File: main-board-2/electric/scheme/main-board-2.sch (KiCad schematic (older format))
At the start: 125 parts, among them K1 power-switch, K2 usb-power-switch, P1 batt, P10 rst, P11 screw-1, P13 screw-2, P14 gpio-big, P15 gpio-small, P16 moto-1, P17 moto-2, P2 CONN_4, P3 trigger-btn, P4 CONN_3X2, P5 reg-short-to-gnd-1, P6 reg-short-to-gnd-2, P7 bootloader, P8 cross board conn, P9 rst, Q1 IRLML2244, Q10 IRLML2244, Q11 sot223, Q12 bc857, Q13 irlml2244, Q2 BC847, Q3 IRLML2244, Q4 IRLML2244, Q5 BC847, Q6 BC847, Q7 BC847, Q8 BC847, Q9 IRLML2244, U1 LM317AEMP, U2 LM317AT, U3 LM317AEMP, U4 LM317AT, U5 LM293, U6 L298, U7 MINI-USB-B, X1 8MHz

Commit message: Routing...
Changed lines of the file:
@@
 Sheet 1 1
 Title "Main board 2"
-Date "9 dec 2013"
+Date "10 dec 2013"
 Rev ""
 Comp ""
@@
 Text Label 17650 4000 0    60   ~ 0
 gnd
-Text Label 14400 7700 0    60   ~ 0
+Text Label 14400 9650 0    60   ~ 0
 gpio-1
-Text Label 14600 4750 0    60   ~ 0
+Text Label 14400 7700 0    60   ~ 0
 gpio-2
-Text Label 14600 4150 0    60   ~ 0
+Text Label 14600 4350 0    60   ~ 0
 gpio-3
-Text Label 14600 3750 0    60   ~ 0
+Text Label 14600 3950 0    60   ~ 0
 gpio-4
 Text Label 14400 10050 0    60   ~ 0
 gpio-5
-Text Label 14600 4550 0    60   ~ 0
+Text Label 14600 4750 0    60   ~ 0
 gpio-6
-Text Label 14600 4350 0    60   ~ 0
+Text Label 14600 4550 0    60   ~ 0
 gpio-7
-Text Label 14600 3950 0    60   ~ 0
+Text Label 14600 4150 0    60   ~ 0
 gpio-8
 Text Label 16150 3300 0    60   ~ 0
@@
 Text Label 17900 4500 0    60   ~ 0
 swd-io
-Text Label 14400 9650 0    60   ~ 0
+Text Label 14600 3750 0    60   ~ 0
 gpio-9
 Text Label 16150 4300 0    60   ~ 0

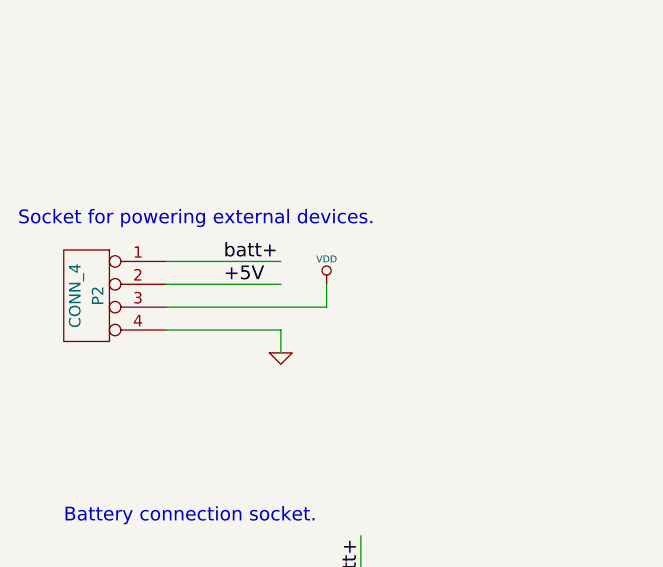
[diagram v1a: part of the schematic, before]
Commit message: Routing. It turnes out it is very nontrivial to route with horizontal TO-220. I'm going to change to vertical TO-220.
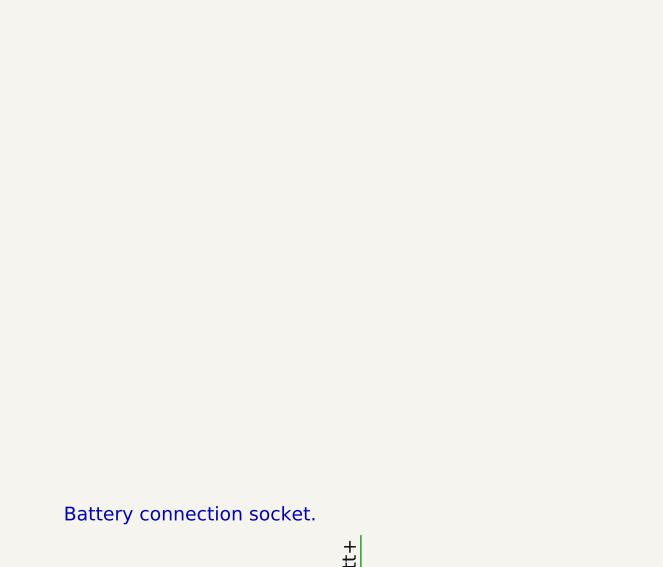
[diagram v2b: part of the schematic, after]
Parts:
- removed P2: CONN_4, symbol CONN_4
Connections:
- wire segments 423 -> 417
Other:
- note removed: "Socket for powering external devices."
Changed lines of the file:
@@
 Text Notes 11300 12800 0    60   ~ 0
 Two unconnected pins for screws.\nThe newest Raspberry Pi contains \nholes for M2.5 screws.
-$Comp
-L CONN_4 P2
-U 1 1 52A0D56C
-P 1350 19950
-F 0 "P2" V 1300 19950 50  0000 C CNN
-F 1 "CONN_4" V 1400 19950 50  0000 C CNN
-F 2 "" H 1350 19950 60  0001 C CNN
-F 3 "" H 1350 19950 60  0001 C CNN
-	1    1350 19950
-	-1   0    0    -1
-$EndComp
-Wire Wire Line
-	1700 19800 2200 19800
-Wire Wire Line
-	1700 19900 2200 19900
-Wire Wire Line
-	1700 20000 2400 20000
-Wire Wire Line
-	1700 20100 2200 20100
-Wire Wire Line
-	2200 20100 2200 20200
-$Comp
-L GND #PWR032
-U 1 1 52A0D577
-P 2200 20200
-F 0 "#PWR032" H 2200 20200 30  0001 C CNN
-F 1 "GND" H 2200 20130 30  0001 C CNN
-F 2 "" H 2200 20200 60  0001 C CNN
-F 3 "" H 2200 20200 60  0001 C CNN
-	1    2200 20200
-	1    0    0    -1
-$EndComp
-Wire Wire Line
-	2400 20000 2400 19900
-$Comp
-L VDD #PWR033
-U 1 1 52A0D57E
-P 2400 19900
-F 0 "#PWR033" H 2400 20000 30  0001 C CNN
-F 1 "VDD" H 2400 20010 30  0000 C CNN
-F 2 "" H 2400 19900 60  0001 C CNN
-F 3 "" H 2400 19900 60  0001 C CNN
-	1    2400 19900
-	1    0    0    -1
-$EndComp
-Text Label 1950 19800 0    60   ~ 0
-batt+
-Text Label 1950 19900 0    60   ~ 0
-+5V
-Text Notes 1050 19650 0    60   ~ 0
-Socket for powering external devices.
 Wire Wire Line
 	14100 7700 15100 7700

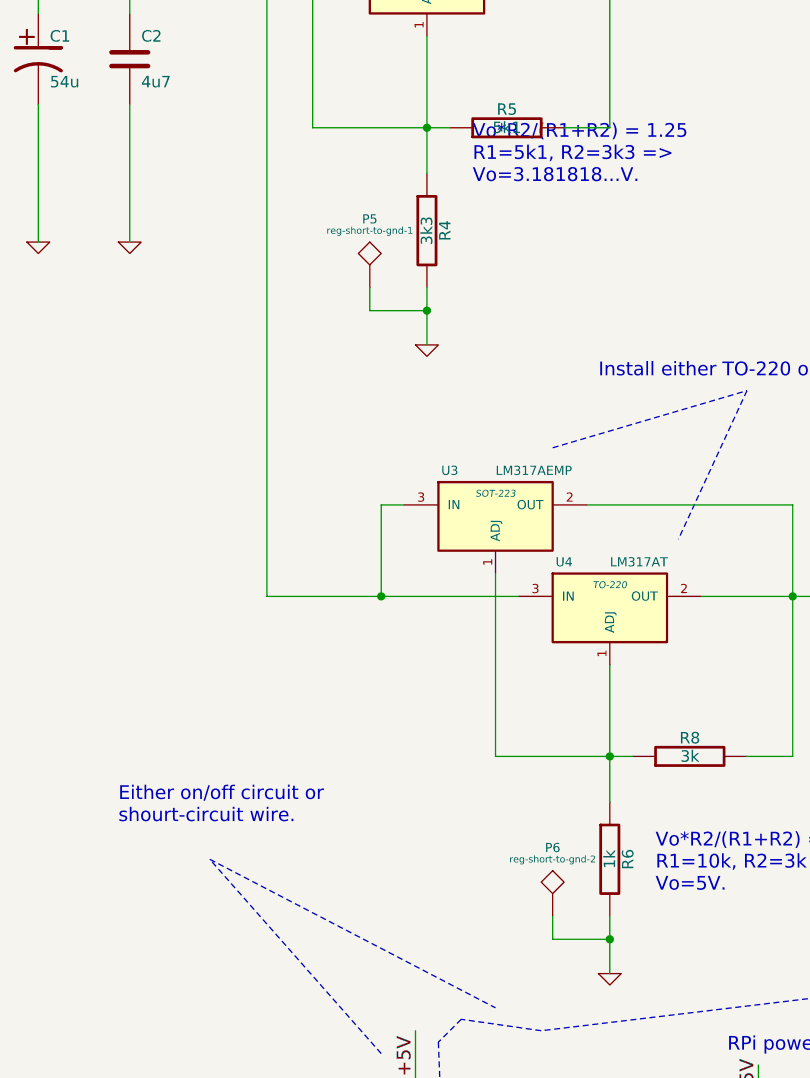
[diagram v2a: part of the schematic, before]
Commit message: Just one more circuit Vdd to addon socket last.
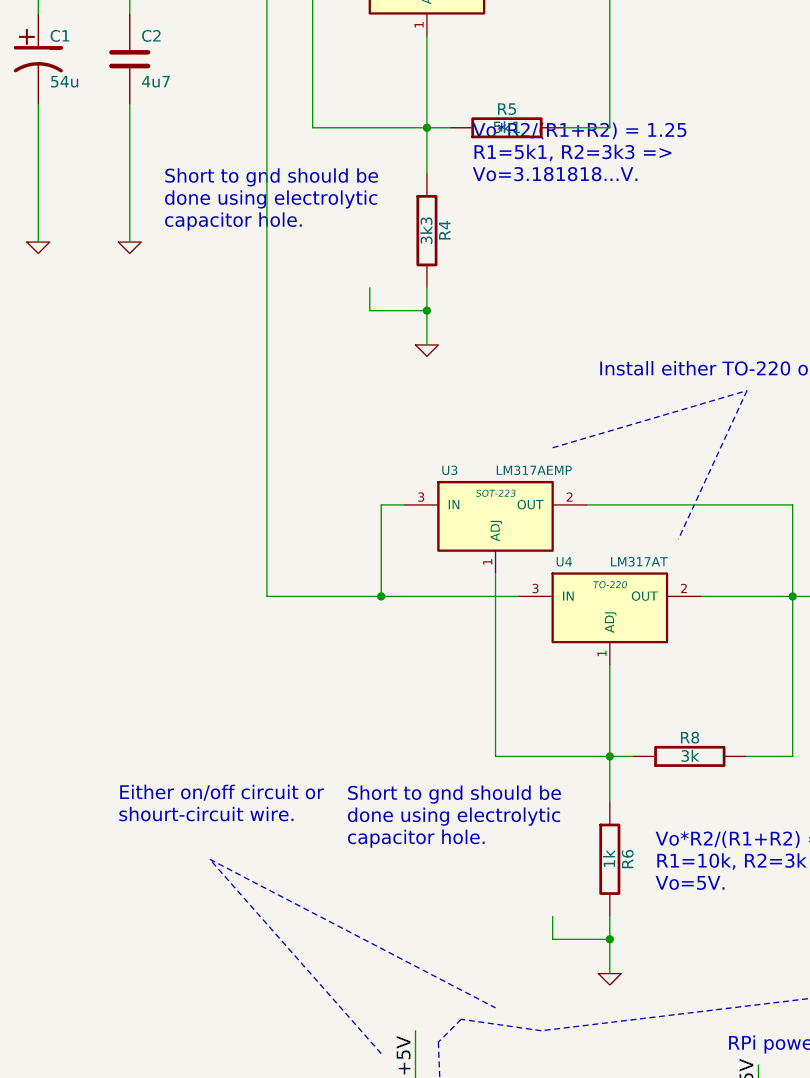
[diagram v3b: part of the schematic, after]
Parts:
- removed P5: reg-short-to-gnd-1, ~, symbol TST
- removed P6: reg-short-to-gnd-2, ~, symbol TST
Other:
- note added: "Short to gnd should be \ndone using electrolytic \ncapacitor hole."
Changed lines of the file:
@@
 Sheet 1 1
 Title "Main board 2"
-Date "10 dec 2013"
+Date "11 dec 2013"
 Rev ""
 Comp ""
@@
 	9450 2500 9450 2600
 $Comp
-L GND #PWR034
+L GND #PWR032
 U 1 1 52A0D5D0
 P 9450 2600
-F 0 "#PWR034" H 9450 2600 30  0001 C CNN
+F 0 "#PWR032" H 9450 2600 30  0001 C CNN
 F 1 "GND" H 9450 2530 30  0001 C CNN
 F 2 "" H 9450 2600 60  0001 C CNN
@@
 	8200 7750 8200 7600
 $Comp
-L VDD #PWR035
+L VDD #PWR033
 U 1 1 52A0E8C5
 P 8200 7600
-F 0 "#PWR035" H 8200 7700 30  0001 C CNN
+F 0 "#PWR033" H 8200 7700 30  0001 C CNN
 F 1 "VDD" H 8200 7710 30  0000 C CNN
 F 2 "" H 8200 7600 60  0001 C CNN
@@
 +5V
 $Comp
-L GND #PWR036
+L GND #PWR034
 U 1 1 52A0FADE
 P 13250 20350
-F 0 "#PWR036" H 13250 20350 30  0001 C CNN
+F 0 "#PWR034" H 13250 20350 30  0001 C CNN
 F 1 "GND" H 13250 20280 30  0001 C CNN
 F 2 "" H 13250 20350 60  0001 C CNN
@@
 addon-vdd
 $Comp
-L VDD #PWR037
+L VDD #PWR035
 U 1 1 52A0FB08
 P 13250 18850
-F 0 "#PWR037" H 13250 18950 30  0001 C CNN
+F 0 "#PWR035" H 13250 18950 30  0001 C CNN
 F 1 "VDD" H 13250 18960 30  0000 C CNN
 F 2 "" H 13250 18850 60  0001 C CNN
@@
 Connection ~ 14300 19000
 $Comp
-L VDD #PWR038
+L VDD #PWR036
 U 1 1 52A105F2
 P 11950 19150
-F 0 "#PWR038" H 11950 19250 30  0001 C CNN
+F 0 "#PWR036" H 11950 19250 30  0001 C CNN
 F 1 "VDD" H 11950 19260 30  0000 C CNN
 F 2 "" H 11950 19150 60  0001 C CNN
@@
 $EndComp
 $Comp
-L GND #PWR039
+L GND #PWR037
 U 1 1 52A1147D
 P 1300 2800
-F 0 "#PWR039" H 1300 2800 30  0001 C CNN
+F 0 "#PWR037" H 1300 2800 30  0001 C CNN
 F 1 "GND" H 1300 2730 30  0001 C CNN
 F 2 "" H 1300 2800 60  0001 C CNN
@@
 $EndComp
 $Comp
-L GND #PWR040
+L GND #PWR038
 U 1 1 52A12B15
 P 5300 5200
-F 0 "#PWR040" H 5300 5200 30  0001 C CNN
+F 0 "#PWR038" H 5300 5200 30  0001 C CNN
 F 1 "GND" H 5300 5130 30  0001 C CNN
 F 2 "" H 5300 5200 60  0001 C CNN
@@
 $EndComp
 $Comp
-L GND #PWR041
+L GND #PWR039
 U 1 1 52A12B21
 P 4950 5200
-F 0 "#PWR041" H 4950 5200 30  0001 C CNN
+F 0 "#PWR039" H 4950 5200 30  0001 C CNN
 F 1 "GND" H 4950 5130 30  0001 C CNN
 F 2 "" H 4950 5200 60  0001 C CNN
@@
 $EndComp
 $Comp
-L GND #PWR042
+L GND #PWR040
 U 1 1 52A12B2D
 P 3800 6000
-F 0 "#PWR042" H 3800 6000 30  0001 C CNN
+F 0 "#PWR040" H 3800 6000 30  0001 C CNN
 F 1 "GND" H 3800 5930 30  0001 C CNN
 F 2 "" H 3800 6000 60  0001 C CNN
@@
 	24000 5050 24000 5100
 $Comp
-L GND #PWR043
+L GND #PWR041
 U 1 1 52A1B75F
 P 24000 5100
-F 0 "#PWR043" H 24000 5100 30  0001 C CNN
+F 0 "#PWR041" H 24000 5100 30  0001 C CNN
 F 1 "GND" H 24000 5030 30  0001 C CNN
 F 2 "" H 24000 5100 60  0001 C CNN
@@
 Connection ~ 30050 5800
 $Comp
-L GND #PWR044
+L GND #PWR042
 U 1 1 52A1DEAF
 P 30050 6000
-F 0 "#PWR044" H 30050 6000 30  0001 C CNN
+F 0 "#PWR042" H 30050 6000 30  0001 C CNN
 F 1 "GND" H 30050 5930 30  0001 C CNN
 F 2 "" H 30050 6000 60  0001 C CNN
@@
 	23350 5850 23350 6000
 $Comp
-L GND #PWR045
+L GND #PWR043
 U 1 1 52A1EAE1
 P 23350 6000
-F 0 "#PWR045" H 23350 6000 30  0001 C CNN
+F 0 "#PWR043" H 23350 6000 30  0001 C CNN
 F 1 "GND" H 23350 5930 30  0001 C CNN
 F 2 "" H 23350 6000 60  0001 C CNN
@@
 $EndComp
 $Comp
-L GND #PWR046
+L GND #PWR044
 U 1 1 52A1A7C0
 P 20700 3450
-F 0 "#PWR046" H 20700 3450 30  0001 C CNN
+F 0 "#PWR044" H 20700 3450 30  0001 C CNN
 F 1 "GND" H 20700 3380 30  0001 C CNN
 F 2 "" H 20700 3450 60  0001 C CNN
@@
 	23350 4750 23350 4900
 $Comp
-L GND #PWR047
+L GND #PWR045
 U 1 1 52A1A7F0
 P 23350 4900
-F 0 "#PWR047" H 23350 4900 30  0001 C CNN
+F 0 "#PWR045" H 23350 4900 30  0001 C CNN
 F 1 "GND" H 23350 4830 30  0001 C CNN
 F 2 "" H 23350 4900 60  0001 C CNN
@@
 addon-pwr-en
 $Comp
-L PWR_FLAG #FLG048
+L PWR_FLAG #FLG046
 U 1 1 52A1DA8C
 P 23350 1800
-F 0 "#FLG048" H 23350 1895 30  0001 C CNN
+F 0 "#FLG046" H 23350 1895 30  0001 C CNN
 F 1 "PWR_FLAG" H 23350 1980 30  0000 C CNN
 F 2 "" H 23350 1800 60  0001 C CNN
@@
 Connection ~ 23050 5250
 $Comp
-L PWR_FLAG #FLG049
+L PWR_FLAG #FLG047
 U 1 1 52A1DD5E
 P 23050 5100
-F 0 "#FLG049" H 23050 5195 30  0001 C CNN
+F 0 "#FLG047" H 23050 5195 30  0001 C CNN
 F 1 "PWR_FLAG" H 23050 5280 30  0000 C CNN
 F 2 "" H 23050 5100 60  0001 C CNN
@@
 	28300 5050 28300 5150
 $Comp
-L GND #PWR050
+L GND #PWR048
 U 1 1 52A1EACD
 P 28300 5150
-F 0 "#PWR050" H 28300 5150 30  0001 C CNN
+F 0 "#PWR048" H 28300 5150 30  0001 C CNN
 F 1 "GND" H 28300 5080 30  0001 C CNN
 F 2 "" H 28300 5150 60  0001 C CNN
@@
 $EndComp
 $Comp
-L PWR_FLAG #FLG051
+L PWR_FLAG #FLG049
 U 1 1 52A1EEED
 P 24800 19400
-F 0 "#FLG051" H 24800 19495 30  0001 C CNN
+F 0 "#FLG049" H 24800 19495 30  0001 C CNN
 F 1 "PWR_FLAG" H 24800 19580 30  0000 C CNN
 F 2 "" H 24800 19400 60  0001 C CNN
@@
 $EndComp
 $Comp
-L GND #PWR052
+L GND #PWR050
 U 1 1 52A1ABD9
 P 4450 7900
-F 0 "#PWR052" H 4450 7900 30  0001 C CNN
+F 0 "#PWR050" H 4450 7900 30  0001 C CNN
 F 1 "GND" H 4450 7830 30  0001 C CNN
 F 2 "" H 4450 7900 60  0001 C CNN
@@
 $EndComp
 $Comp
-L GND #PWR053
+L GND #PWR051
 U 1 1 52A1AC0E
 P 5500 8200
-F 0 "#PWR053" H 5500 8200 30  0001 C CNN
+F 0 "#PWR051" H 5500 8200 30  0001 C CNN
 F 1 "GND" H 5500 8130 30  0001 C CNN
 F 2 "" H 5500 8200 60  0001 C CNN
@@
 Wire Wire Line
 	3300 4250 3300 5050
-$Comp
-L TST P5
-U 1 1 52A32BAB
-P 2750 3000
-F 0 "P5" H 2750 3300 40  0000 C CNN
-F 1 "reg-short-to-gnd-1" H 2750 3250 30  0000 C CNN
-F 2 "~" H 2750 3000 60  0000 C CNN
-F 3 "~" H 2750 3000 60  0000 C CNN
-	1    2750 3000
-	1    0    0    -1
-$EndComp
 Wire Wire Line
 	2750 3000 2750 3100
@@
 	2750 3100 3000 3100
 Connection ~ 3000 3100
-$Comp
-L TST P6
-U 1 1 52A32D31
-P 3550 5750
-F 0 "P6" H 3550 6050 40  0000 C CNN
-F 1 "reg-short-to-gnd-2" H 3550 6000 30  0000 C CNN
-F 2 "~" H 3550 5750 60  0000 C CNN
-F 3 "~" H 3550 5750 60  0000 C CNN
-	1    3550 5750
-	1    0    0    -1
-$EndComp
 Wire Wire Line
 	3550 5750 3550 5850
@@
 +5V
 $Comp
-L VDD #PWR054
+L VDD #PWR052
 U 1 1 52A348A1
 P 11700 18600
-F 0 "#PWR054" H 11700 18700 30  0001 C CNN
+F 0 "#PWR052" H 11700 18700 30  0001 C CNN
 F 1 "VDD" H 11700 18710 30  0000 C CNN
 F 2 "" H 11700 18600 60  0001 C CNN
@@
 Connection ~ 29850 19250
 $Comp
-L GND #PWR055
+L GND #PWR053
 U 1 1 52A36BFA
 P 29850 20300
-F 0 "#PWR055" H 29850 20300 30  0001 C CNN
+F 0 "#PWR053" H 29850 20300 30  0001 C CNN
 F 1 "GND" H 29850 20230 30  0001 C CNN
 F 2 "" H 29850 20300 60  0000 C CNN
@@
 	25200 10000 25200 9900
 $Comp
-L VDD #PWR056
+L VDD #PWR054
 U 1 1 52A3B630
 P 25200 9900
-F 0 "#PWR056" H 25200 10000 30  0001 C CNN
+F 0 "#PWR054" H 25200 10000 30  0001 C CNN
 F 1 "VDD" H 25200 10010 30  0000 C CNN
 F 2 "" H 25200 9900 60  0001 C CNN
@@
 	25200 10800 25200 10900
 $Comp
-L GND #PWR057
+L GND #PWR055
 U 1 1 52A3B7FD
 P 25200 10900
-F 0 "#PWR057" H 25200 10900 30  0001 C CNN
+F 0 "#PWR055" H 25200 10900 30  0001 C CNN
 F 1 "GND" H 25200 10830 30  0001 C CNN
 F 2 "" H 25200 10900 60  0001 C CNN
@@
 Connection ~ 24150 11350
 $Comp
-L GND #PWR058
+L GND #PWR056
 U 1 1 52A3CFE1
 P 24150 11450
-F 0 "#PWR058" H 24150 11450 30  0001 C CNN
+F 0 "#PWR056" H 24150 11450 30  0001 C CNN
 F 1 "GND" H 24150 11380 30  0001 C CNN
 F 2 "" H 24150 11450 60  0001 C CNN
@@
 	24650 11150 24650 11450
 $Comp
-L GND #PWR059
+L GND #PWR057
 U 1 1 52A3D75D
 P 24650 11450
-F 0 "#PWR059" H 24650 11450 30  0001 C CNN
+F 0 "#PWR057" H 24650 11450 30  0001 C CNN
 F 1 "GND" H 24650 11380 30  0001 C CNN
 F 2 "" H 24650 11450 60  0001 C CNN
@@
 	24650 9700 24650 9600
 $Comp
-L VDD #PWR060
+L VDD #PWR058
 U 1 1 52A3D93E
 P 24650 9600
-F 0 "#PWR060" H 24650 9700 30  0001 C CNN
+F 0 "#PWR058" H 24650 9700 30  0001 C CNN
 F 1 "VDD" H 24650 9710 30  0000 C CNN
 F 2 "" H 24650 9600 60  0001 C CNN
@@
 	25100 13800 25100 13700
 $Comp
-L VDD #PWR061
+L VDD #PWR059
 U 1 1 52A41118
 P 25100 13700
-F 0 "#PWR061" H 25100 13800 30  0001 C CNN
+F 0 "#PWR059" H 25100 13800 30  0001 C CNN
 F 1 "VDD" H 25100 13810 30  0000 C CNN
 F 2 "" H 25100 13700 60  0001 C CNN
@@
 	25100 14600 25100 14700
 $Comp
-L GND #PWR062
+L GND #PWR060
 U 1 1 52A4111F
 P 25100 14700
-F 0 "#PWR062" H 25100 14700 30  0001 C CNN
+F 0 "#PWR060" H 25100 14700 30  0001 C CNN
 F 1 "GND" H 25100 14630 30  0001 C CNN
 F 2 "" H 25100 14700 60  0001 C CNN
@@
 Connection ~ 24050 15150
 $Comp
-L GND #PWR063
+L GND #PWR061
 U 1 1 52A41146
 P 24050 15250
-F 0 "#PWR063" H 24050 15250 30  0001 C CNN
+F 0 "#PWR061" H 24050 15250 30  0001 C CNN
 F 1 "GND" H 24050 15180 30  0001 C CNN
 F 2 "" H 24050 15250 60  0001 C CNN
@@
 	24550 14950 24550 15250
 $Comp
-L GND #PWR064
+L GND #PWR062
 U 1 1 52A4115C
 P 24550 15250
-F 0 "#PWR064" H 24550 15250 30  0001 C CNN
+F 0 "#PWR062" H 24550 15250 30  0001 C CNN
 F 1 "GND" H 24550 15180 30  0001 C CNN
 F 2 "" H 24550 15250 60  0001 C CNN
@@
 	24550 13500 24550 13400
 $Comp
-L VDD #PWR065
+L VDD #PWR063
 U 1 1 52A41163
 P 24550 13400
-F 0 "#PWR065" H 24550 13500 30  0001 C CNN
+F 0 "#PWR063" H 24550 13500 30  0001 C CNN
 F 1 "VDD" H 24550 13510 30  0000 C CNN
 F 2 "" H 24550 13400 60  0001 C CNN
@@
 	15900 3500 15900 3700
 $Comp
-L GND #PWR066
+L GND #PWR064
 U 1 1 52A37283
 P 15900 3700
-F 0 "#PWR066" H 15900 3700 30  0001 C CNN
+F 0 "#PWR064" H 15900 3700 30  0001 C CNN
 F 1 "GND" H 15900 3630 30  0001 C CNN
 F 2 "" H 15900 3700 60  0001 C CNN
@@
 Text Label 17650 4100 0    60   ~ 0
 pwrVs
+Text Notes 2650 5450 0    60   ~ 0
+Short to gnd should be \ndone using electrolytic \ncapacitor hole.
+Text Notes 1850 2750 0    60   ~ 0
+Short to gnd should be \ndone using electrolytic \ncapacitor hole.
 $EndSCHEMATC
